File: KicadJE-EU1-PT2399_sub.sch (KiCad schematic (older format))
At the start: 49 parts

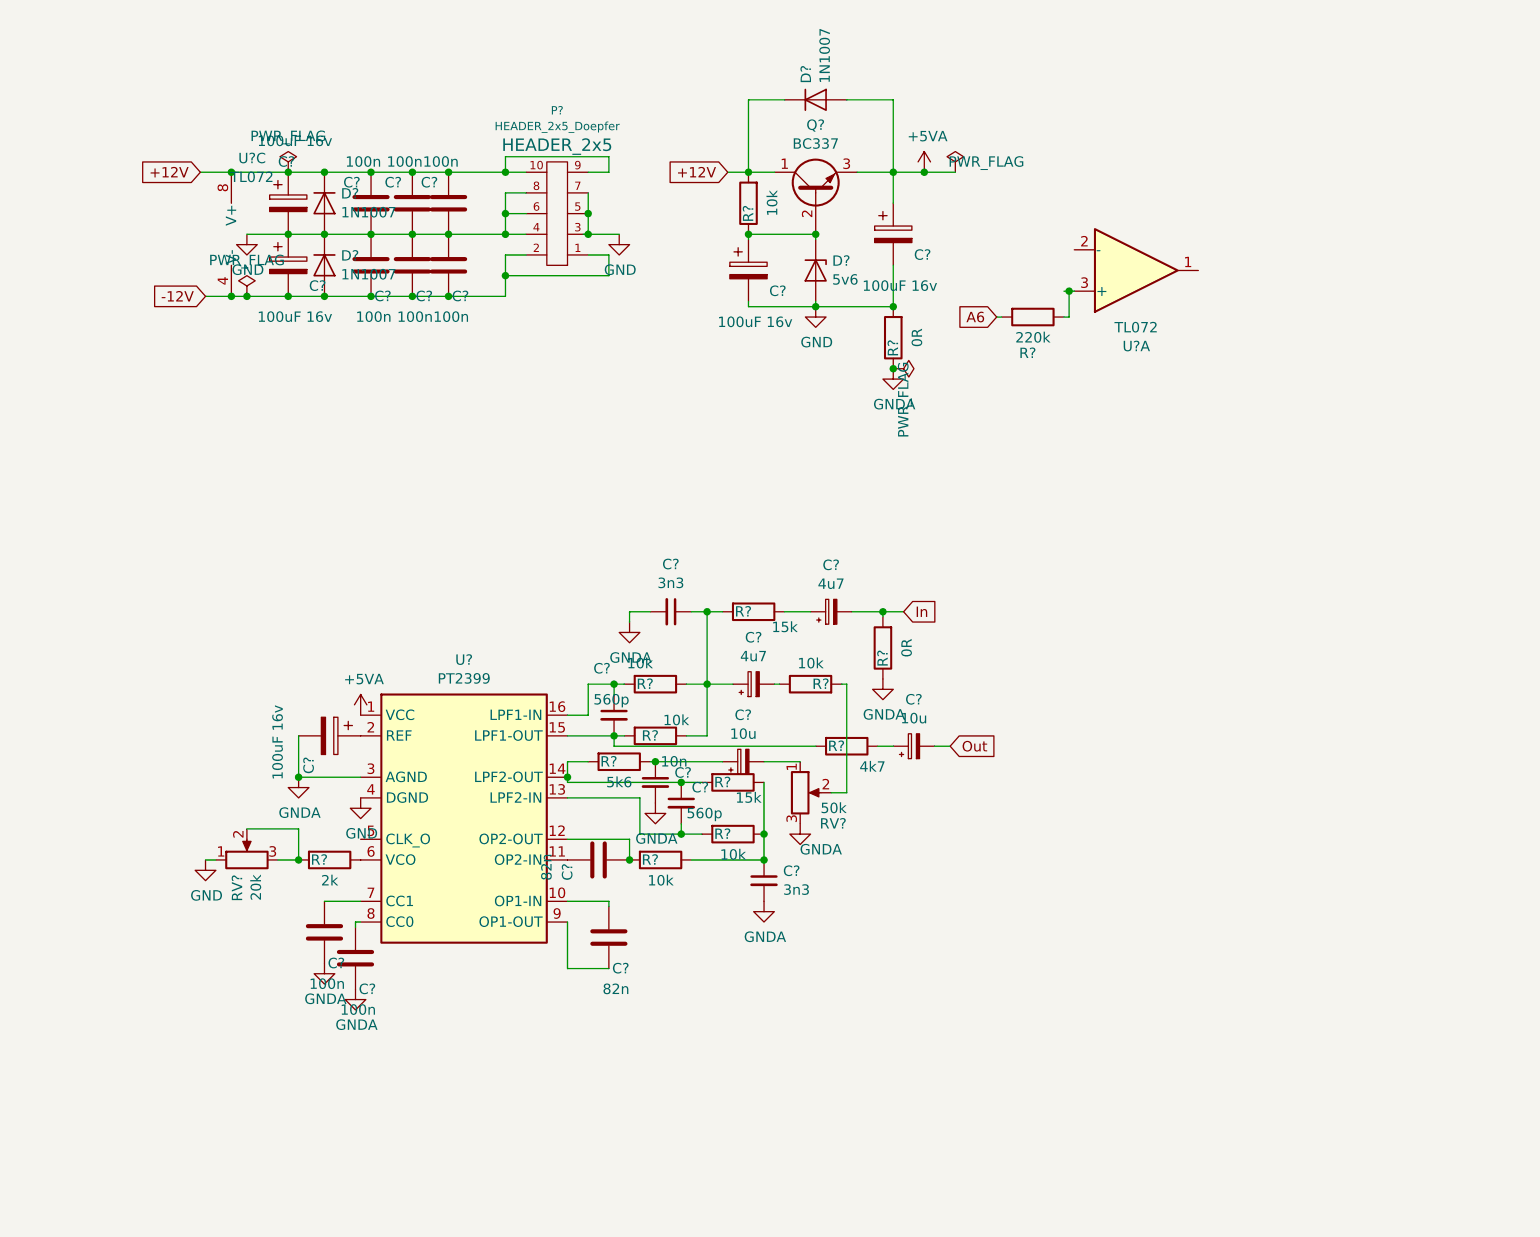
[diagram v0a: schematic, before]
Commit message: anti latchup initiated
inspiration:
https://www.electrosmash.com/images/tech/pt2399/PT2399_Transistor_Current_Sink_Pin6.png
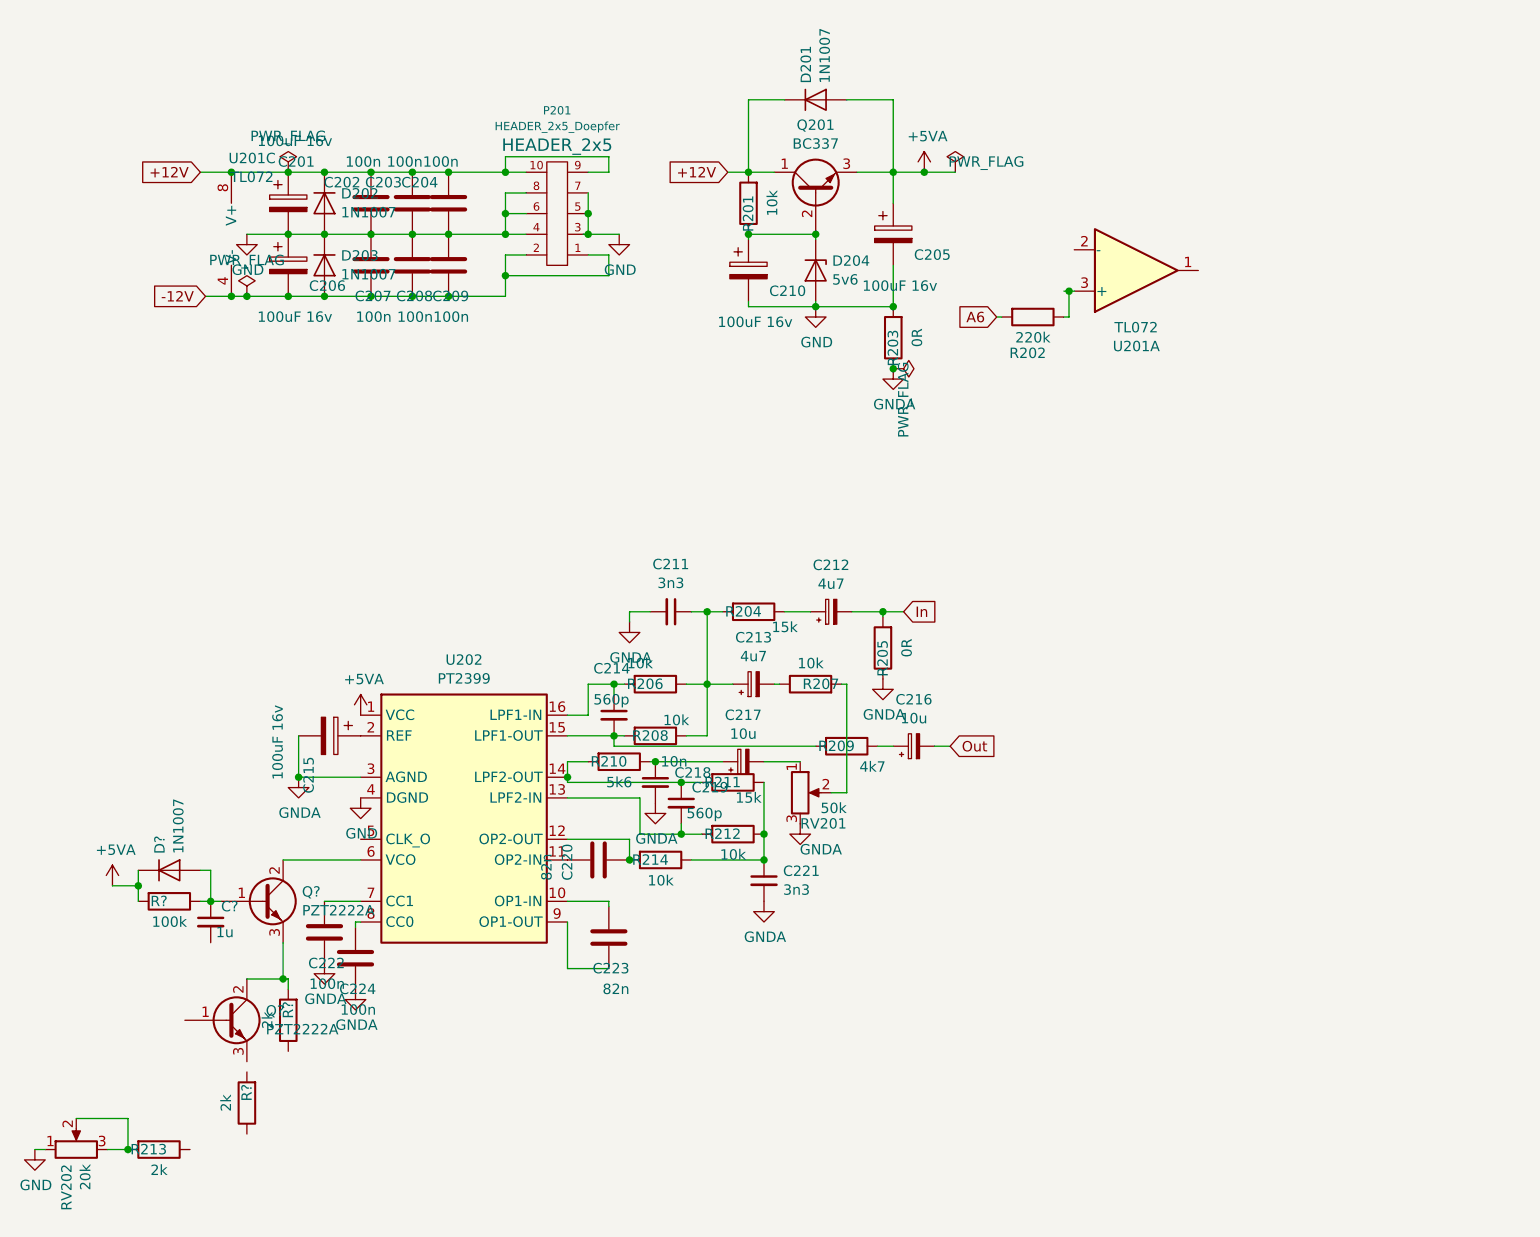
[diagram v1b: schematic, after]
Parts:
- added C?: 1u, symbol Device:C_Small
- added D?: 1N1007, Diode_SMD:D_SOD-123, symbol Device:D
- added Q? (x2): PZT2222A, Package_TO_SOT_SMD:SOT-223, symbol Transistor_BJT:PZT2222A
- added R?: 100k, Resistor_SMD:R_0805_2012Metric_Pad1.15x1.40mm_HandSolder, symbol Device:R
- added R? (x2): 2k, Resistor_SMD:R_0805_2012Metric_Pad1.15x1.40mm_HandSolder, symbol Device:R
- gave numbers to parts that had none: 48
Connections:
- net +5VA: now also D?.1 (K), R?.2
- net at U202.6 (VCO): now also Q?.2 (C); no longer R213.1
- new net: C?.1, D?.2 (A), Q?.1 (B), R?.1
- new net: Q?.2 (C), Q?.3 (E), R?.2
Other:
- moved on the sheet: R213, RV202

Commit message: Basic circuit done
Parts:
- removed R202: 220k, Resistor_SMD:R_0805_2012Metric_Pad1.15x1.40mm_HandSolder, symbol Device:R
- removed unit 1 of U201
- added C226: 100n, Capacitor_SMD:C_0805_2012Metric_Pad1.15x1.40mm_HandSolder, symbol Device:C
- R214: renamed from R213; value 2k -> 120k
- R215: renamed from R?; value 2k -> 22k
- R216: renamed from R?; value 2k -> 150R
- gave numbers to parts that had none: 5
- renumbered C222 to C223, C223 to C224, C224 to C225, R203 to R202, R204 to R203, R205 to R204, R206 to R205, R207 to R206, R208 to R207, R209 to R208, R210 to R209, R211 to R210, R212 to R211, R214 to R212
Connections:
- net +5VA: now also R214.2
- net GND: now also C222.2, RV202.3; no longer RV202.1
- net GNDA: now also R216.1, C226.1
- net at R214.1: now also RV202.1
- net at Q203.1 (B): now also RV202.2, C226.2
- net at Q203.3 (E): now also R215.1, R216.2
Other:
- note added: "22k = 290ms\napprox max"
- note added: "Anti latchup\n100K*1u = 1s"
- note added: "Voltage divider for \nVbe between 0 \nand 0,65v on the input"
- moved on the sheet: C211, C212, C213, C214, C215, C216, C217, C218, C219, C220, C221, C222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

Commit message: more footprints
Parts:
- added J201: In, AJ-Dropbox-Kicad:PJ301SM, symbol Connector:AudioJack2
- added J202: Out, AJ-Dropbox-Kicad:PJ301SM, symbol Connector:AudioJack2
- C211, C212, C213, C214, C216, C217, C218, C219, C221, C222: footprint (none) -> Capacitor_SMD:C_0805_2012Metric_Pad1.15x1.40mm_HandSolder
- P201: footprint HEADER_2x5 -> Connector_PinHeader_2.54mm:PinHeader_2x05_P2.54mm_Vertical
- Q202, Q203: footprint Package_TO_SOT_SMD:SOT-223 -> Package_TO_SOT_SMD:SOT-23
- U202: footprint (none) -> Package_DIP:DIP-16_W7.62mm
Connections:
- net GND: now also J201.S, J202.S
- net In: now also J201.T
- net Out: now also J202.T
- net +12V renamed +12Vb
- net -12V renamed -12Vb
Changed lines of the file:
@@
 	1300 1750 1500 1750
 Text GLabel 1100 1750 0    50   Input ~ 0
--12V
+-12Vb
 Text GLabel 1075 1150 0    50   Input ~ 0
-+12V
++12Vb
 $Comp
 L Device:C C?
@@
 F 0 "P201" H 2800 852 40  0000 C CNN
 F 1 "HEADER_2x5_Doepfer" H 2800 928 40  0000 C CNN
-F 2 "HEADER_2x5" H 2800 1019 60  0000 C CNN
+F 2 "Connector_PinHeader_2.54mm:PinHeader_2x05_P2.54mm_Vertical" H 2800 1019 60  0000 C CNN
 F 3 "" H 2800 1350 60  0000 C CNN
 	1    2800 1350
@@
 	2950 1450 3100 1450
 Text GLabel 3625 1150 0    50   Input ~ 0
-+12V
++12Vb
 Wire Wire Line
 	3625 1150 3725 1150
@@
 F 0 "U202" H 4225 4817 50  0000 C CNN
 F 1 "PT2399" H 4225 4726 50  0000 C CNN
-F 2 "" H 4225 3650 50  0001 C CNN
+F 2 "Package_DIP:DIP-16_W7.62mm" H 4225 3650 50  0001 C CNN
 F 3 "http://sound.westhost.com/pt2399.pdf" H 4225 3650 50  0001 C CNN
 	1    4225 4050
@@
 $EndComp
 $Comp
-L power:+5VA #PWR0208
+L power:+5VA #PWR0209
 U 1 1 5D64D016
 P 3725 3550
-F 0 "#PWR0208" H 3725 3400 50  0001 C CNN
+F 0 "#PWR0209" H 3725 3400 50  0001 C CNN
 F 1 "+5VA" H 3740 3723 50  0000 C CNN
 F 2 "" H 3725 3550 50  0001 C CNN
@@
 Connection ~ 4425 1800
 $Comp
-L power:GNDA #PWR0205
+L power:GNDA #PWR0206
 U 1 1 5D64E4DB
 P 4425 2100
-F 0 "#PWR0205" H 4425 1850 50  0001 C CNN
+F 0 "#PWR0206" H 4425 1850 50  0001 C CNN
 F 1 "GNDA" H 4430 1927 50  0000 C CNN
 F 2 "" H 4425 2100 50  0001 C CNN
@@
 Connection ~ 4425 2100
 $Comp
-L power:GNDA #PWR0209
+L power:GNDA #PWR0210
 U 1 1 5D64E67F
 P 3425 3850
-F 0 "#PWR0209" H 3425 3600 50  0001 C CNN
+F 0 "#PWR0210" H 3425 3600 50  0001 C CNN
 F 1 "GNDA" H 3430 3677 50  0000 C CNN
 F 2 "" H 3425 3850 50  0001 C CNN
@@
 P 3725 3950
 AR Path="/5D64E6E6" Ref="#PWR?"  Part="1"
-AR Path="/5D60ED9A/5D64E6E6" Ref="#PWR0210"  Part="1"
-F 0 "#PWR0210" H 3725 3700 50  0001 C CNN
+AR Path="/5D60ED9A/5D64E6E6" Ref="#PWR0211"  Part="1"
+F 0 "#PWR0211" H 3725 3700 50  0001 C CNN
 F 1 "GND" H 3730 3777 50  0000 C CNN
 F 2 "" H 3725 3950 50  0001 C CNN
@@
 P 2450 5250
 AR Path="/5D650219" Ref="#PWR?"  Part="1"
-AR Path="/5D60ED9A/5D650219" Ref="#PWR0218"  Part="1"
-F 0 "#PWR0218" H 2450 5000 50  0001 C CNN
+AR Path="/5D60ED9A/5D650219" Ref="#PWR0219"  Part="1"
+F 0 "#PWR0219" H 2450 5000 50  0001 C CNN
 F 1 "GND" H 2455 5077 50  0000 C CNN
 F 2 "" H 2450 5250 50  0001 C CNN
@@
 	3725 4450 3550 4450
 $Comp
-L power:GNDA #PWR0217
+L power:GNDA #PWR0218
 U 1 1 5D653327
 P 3700 4875
-F 0 "#PWR0217" H 3700 4625 50  0001 C CNN
+F 0 "#PWR0218" H 3700 4625 50  0001 C CNN
 F 1 "GNDA" H 3705 4702 50  0000 C CNN
 F 2 "" H 3700 4875 50  0001 C CNN
@@
 $EndComp
 $Comp
-L power:GNDA #PWR0216
+L power:GNDA #PWR0217
 U 1 1 5D653368
 P 3550 4750
-F 0 "#PWR0216" H 3550 4500 50  0001 C CNN
+F 0 "#PWR0217" H 3550 4500 50  0001 C CNN
 F 1 "GNDA" H 3555 4577 50  0000 C CNN
 F 2 "" H 3550 4750 50  0001 C CNN
@@
 F 0 "C219" H 5325 4050 50  0000 L CNN
 F 1 "560p" H 5300 3925 50  0000 L CNN
-F 2 "" H 5275 3975 50  0001 C CNN
+F 2 "Capacitor_SMD:C_0805_2012Metric_Pad1.15x1.40mm_HandSolder" H 5275 3975 50  0001 C CNN
 F 3 "~" H 5275 3975 50  0001 C CNN
 	1    5275 3975
@@
 F 0 "C221" H 5767 4396 50  0000 L CNN
 F 1 "3n3" H 5767 4305 50  0000 L CNN
-F 2 "" H 5675 4350 50  0001 C CNN
+F 2 "Capacitor_SMD:C_0805_2012Metric_Pad1.15x1.40mm_HandSolder" H 5675 4350 50  0001 C CNN
 F 3 "~" H 5675 4350 50  0001 C CNN
 	1    5675 4350
@@
 Connection ~ 5675 4250
 $Comp
-L power:GNDA #PWR0214
+L power:GNDA #PWR0215
 U 1 1 5D6610CC
 P 5675 4450
-F 0 "#PWR0214" H 5675 4200 50  0001 C CNN
+F 0 "#PWR0215" H 5675 4200 50  0001 C CNN
 F 1 "GNDA" H 5680 4277 50  0000 C CNN
 F 2 "" H 5675 4450 50  0001 C CNN
@@
 F 0 "C218" H 5242 3921 50  0000 L CNN
 F 1 "10n" H 5175 3975 50  0000 L CNN
-F 2 "" H 5150 3875 50  0001 C CNN
+F 2 "Capacitor_SMD:C_0805_2012Metric_Pad1.15x1.40mm_HandSolder" H 5150 3875 50  0001 C CNN
 F 3 "~" H 5150 3875 50  0001 C CNN
 	1    5150 3875
@@
 $EndComp
 $Comp
-L power:GNDA #PWR0211
+L power:GNDA #PWR0212
 U 1 1 5D667A82
 P 5150 3975
-F 0 "#PWR0211" H 5150 3725 50  0001 C CNN
+F 0 "#PWR0212" H 5150 3725 50  0001 C CNN
 F 1 "GNDA" H 5155 3802 50  0000 C CNN
 F 2 "" H 5150 3975 50  0001 C CNN
@@
 F 0 "C217" V 5800 3775 50  0000 C CNN
 F 1 "10u" V 5709 3775 50  0000 C CNN
-F 2 "" H 5575 3775 50  0001 C CNN
+F 2 "Capacitor_SMD:C_0805_2012Metric_Pad1.15x1.40mm_HandSolder" H 5575 3775 50  0001 C CNN
 F 3 "~" H 5575 3775 50  0001 C CNN
 	1    5575 3775
@@
 	5675 3775 5850 3775
 $Comp
-L power:GNDA #PWR0212
+L power:GNDA #PWR0213
 U 1 1 5D66F427
 P 5850 4075
-F 0 "#PWR0212" H 5850 3825 50  0001 C CNN
+F 0 "#PWR0213" H 5850 3825 50  0001 C CNN
 F 1 "GNDA" H 5950 3950 50  0000 C CNN
 F 2 "" H 5850 4075 50  0001 C CNN
@@
 F 0 "C213" V 5850 3400 50  0000 C CNN
 F 1 "4u7" V 5759 3400 50  0000 C CNN
-F 2 "" H 5625 3400 50  0001 C CNN
+F 2 "Capacitor_SMD:C_0805_2012Metric_Pad1.15x1.40mm_HandSolder" H 5625 3400 50  0001 C CNN
 F 3 "~" H 5625 3400 50  0001 C CNN
 	1    5625 3400
@@
 F 0 "C214" H 4850 3775 50  0000 L CNN
 F 1 "560p" H 4850 3625 50  0000 L CNN
-F 2 "" H 4950 3550 50  0001 C CNN
+F 2 "Capacitor_SMD:C_0805_2012Metric_Pad1.15x1.40mm_HandSolder" H 4950 3550 50  0001 C CNN
 F 3 "~" H 4950 3550 50  0001 C CNN
 	1    4950 3550
@@
 F 0 "C212" V 6225 3050 50  0000 C CNN
 F 1 "4u7" V 6134 3050 50  0000 C CNN
-F 2 "" H 6000 3050 50  0001 C CNN
+F 2 "Capacitor_SMD:C_0805_2012Metric_Pad1.15x1.40mm_HandSolder" H 6000 3050 50  0001 C CNN
 F 3 "~" H 6000 3050 50  0001 C CNN
 	1    6000 3050
@@
 F 0 "C211" V 4996 3050 50  0000 C CNN
 F 1 "3n3" V 5087 3050 50  0000 C CNN
-F 2 "" H 5225 3050 50  0001 C CNN
+F 2 "Capacitor_SMD:C_0805_2012Metric_Pad1.15x1.40mm_HandSolder" H 5225 3050 50  0001 C CNN
 F 3 "~" H 5225 3050 50  0001 C CNN
 	1    5225 3050
@@
 $EndComp
 $Comp
-L power:GNDA #PWR0206
+L power:GNDA #PWR0207
 U 1 1 5D6945A7
 P 5025 3100
-F 0 "#PWR0206" H 5025 2850 50  0001 C CNN
+F 0 "#PWR0207" H 5025 2850 50  0001 C CNN
 F 1 "GNDA" H 5030 2927 50  0000 C CNN
 F 2 "" H 5025 3100 50  0001 C CNN
@@
 $EndComp
 $Comp
-L power:GNDA #PWR0207
+L power:GNDA #PWR0208
 U 1 1 5D694740
 P 6250 3375
-F 0 "#PWR0207" H 6250 3125 50  0001 C CNN
+F 0 "#PWR0208" H 6250 3125 50  0001 C CNN
 F 1 "GNDA" H 6255 3202 50  0000 C CNN
 F 2 "" H 6250 3375 50  0001 C CNN
@@
 F 0 "C216" V 6625 3700 50  0000 C CNN
 F 1 "10u" V 6534 3700 50  0000 C CNN
-F 2 "" H 6400 3700 50  0001 C CNN
+F 2 "Capacitor_SMD:C_0805_2012Metric_Pad1.15x1.40mm_HandSolder" H 6400 3700 50  0001 C CNN
 F 3 "~" H 6400 3700 50  0001 C CNN
 	1    6400 3700
@@
 	6225 3700 6300 3700
 Wire Wire Line
-	6500 3700 6575 3700
-Wire Wire Line
 	4950 3650 4950 3700
 Wire Wire Line
@@
 F 0 "Q202" H 3441 4496 50  0000 L CNN
 F 1 "PZT2222A" H 3441 4405 50  0000 L CNN
-F 2 "Package_TO_SOT_SMD:SOT-223" H 3450 4375 50  0001 L CIN
+F 2 "Package_TO_SOT_SMD:SOT-23" H 3450 4375 50  0001 L CIN
 F 3 "http://www.fairchildsemi.com/ds/PN/PN2222A.pdf" H 3250 4450 50  0001 L CNN
 	1    3250 4450
@@
 F 0 "C222" H 3050 4625 50  0000 L CNN
 F 1 "1u" H 3025 4500 50  0000 L CNN
-F 2 "" H 3000 4550 50  0001 C CNN
+F 2 "Capacitor_SMD:C_0805_2012Metric_Pad1.15x1.40mm_HandSolder" H 3000 4550 50  0001 C CNN
 F 3 "~" H 3000 4550 50  0001 C CNN
 	1    3000 4550
@@
 	2650 4300 2650 4375
 $Comp
-L power:+5VA #PWR0213
+L power:+5VA #PWR0214
 U 1 1 5D6D7FCA
 P 2525 4375
-F 0 "#PWR0213" H 2525 4225 50  0001 C CNN
+F 0 "#PWR0214" H 2525 4225 50  0001 C CNN
 F 1 "+5VA" H 2540 4548 50  0000 C CNN
 F 2 "" H 2525 4375 50  0001 C CNN
@@
 F 0 "Q203" H 3125 5025 50  0000 L CNN
 F 1 "PZT2222A" H 2800 5175 50  0000 L CNN
-F 2 "Package_TO_SOT_SMD:SOT-223" H 3275 4950 50  0001 L CIN
+F 2 "Package_TO_SOT_SMD:SOT-23" H 3275 4950 50  0001 L CIN
 F 3 "http://www.fairchildsemi.com/ds/PN/PN2222A.pdf" H 3075 5025 50  0001 L CNN
 	1    3075 5025
@@
 	2825 5575 3050 5575
 $Comp
-L power:GNDA #PWR0219
+L power:GNDA #PWR0220
 U 1 1 5C5F26D3
 P 3050 5575
-F 0 "#PWR0219" H 3050 5325 50  0001 C CNN
+F 0 "#PWR0220" H 3050 5325 50  0001 C CNN
 F 1 "GNDA" H 3055 5402 50  0000 C CNN
 F 2 "" H 3050 5575 50  0001 C CNN
@@
 P 3000 4650
 AR Path="/5C60BCB0" Ref="#PWR?"  Part="1"
-AR Path="/5D60ED9A/5C60BCB0" Ref="#PWR0215"  Part="1"
-F 0 "#PWR0215" H 3000 4400 50  0001 C CNN
+AR Path="/5D60ED9A/5C60BCB0" Ref="#PWR0216"  Part="1"
+F 0 "#PWR0216" H 3000 4400 50  0001 C CNN
 F 1 "GND" H 3005 4477 50  0000 C CNN
 F 2 "" H 3000 4650 50  0001 C CNN
@@
 Text Notes 3325 5375 0    50   ~ 0
 22k = 290ms\napprox max
+Wire Wire Line
+	6500 3700 6575 3700
+$Comp
+L Connector:AudioJack2 J?
+U 1 1 5C68B7CC
+P 7025 1300
+AR Path="/5C68B7CC" Ref="J?"  Part="1"
+AR Path="/5D60ED9A/5C68B7CC" Ref="J201"  Part="1"
+F 0 "J201" H 6792 1371 50  0000 R CNN
+F 1 "In" H 6792 1280 50  0000 R CNN
+F 2 "AJ-Dropbox-Kicad:PJ301SM" H 7025 1300 50  0001 C CNN
+F 3 "~" H 7025 1300 50  0001 C CNN
+	1    7025 1300
+	-1   0    0    -1
+$EndComp
+$Comp
+L Connector:AudioJack2 J?
+U 1 1 5C68B7D3
+P 7025 1700
+AR Path="/5C68B7D3" Ref="J?"  Part="1"
+AR Path="/5D60ED9A/5C68B7D3" Ref="J202"  Part="1"
+F 0 "J202" H 6792 1771 50  0000 R CNN
+F 1 "Out" H 6792 1680 50  0000 R CNN
+F 2 "AJ-Dropbox-Kicad:PJ301SM" H 7025 1700 50  0001 C CNN
+F 3 "~" H 7025 1700 50  0001 C CNN
+	1    7025 1700
+	-1   0    0    -1
+$EndComp
+Wire Wire Line
+	6525 1700 6825 1700
+Wire Wire Line
+	6525 1300 6825 1300
+Wire Wire Line
+	6825 1200 6675 1200
+Wire Wire Line
+	6825 1600 6675 1600
+Wire Wire Line
+	6675 1800 6675 1600
+Connection ~ 6675 1600
+Wire Wire Line
+	6675 1200 6675 1600
+$Comp
+L power:GND #PWR?
+U 1 1 5C68B7E3
+P 6675 1800
+AR Path="/5C68B7E3" Ref="#PWR?"  Part="1"
+AR Path="/5D60ED9A/5C68B7E3" Ref="#PWR0205"  Part="1"
+F 0 "#PWR0205" H 6675 1550 50  0001 C CNN
+F 1 "GND" H 6680 1627 50  0000 C CNN
+F 2 "" H 6675 1800 50  0001 C CNN
+F 3 "" H 6675 1800 50  0001 C CNN
+	1    6675 1800
+	1    0    0    -1
+$EndComp
+Text GLabel 6525 1300 0    50   Input ~ 0
+In
+Text GLabel 6525 1700 0    50   Input ~ 0
+Out
 $EndSCHEMATC
